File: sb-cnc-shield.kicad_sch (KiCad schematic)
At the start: 62 parts, among them P1 XMOT, P2 YMOT, P3 ZMOT, P4 AMOT, P5 UART, P6 I2C, P7 ES_SETUP, P8 12V-36V, SW1 RESET, U1 ARDUINO_UNO_SHIELD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

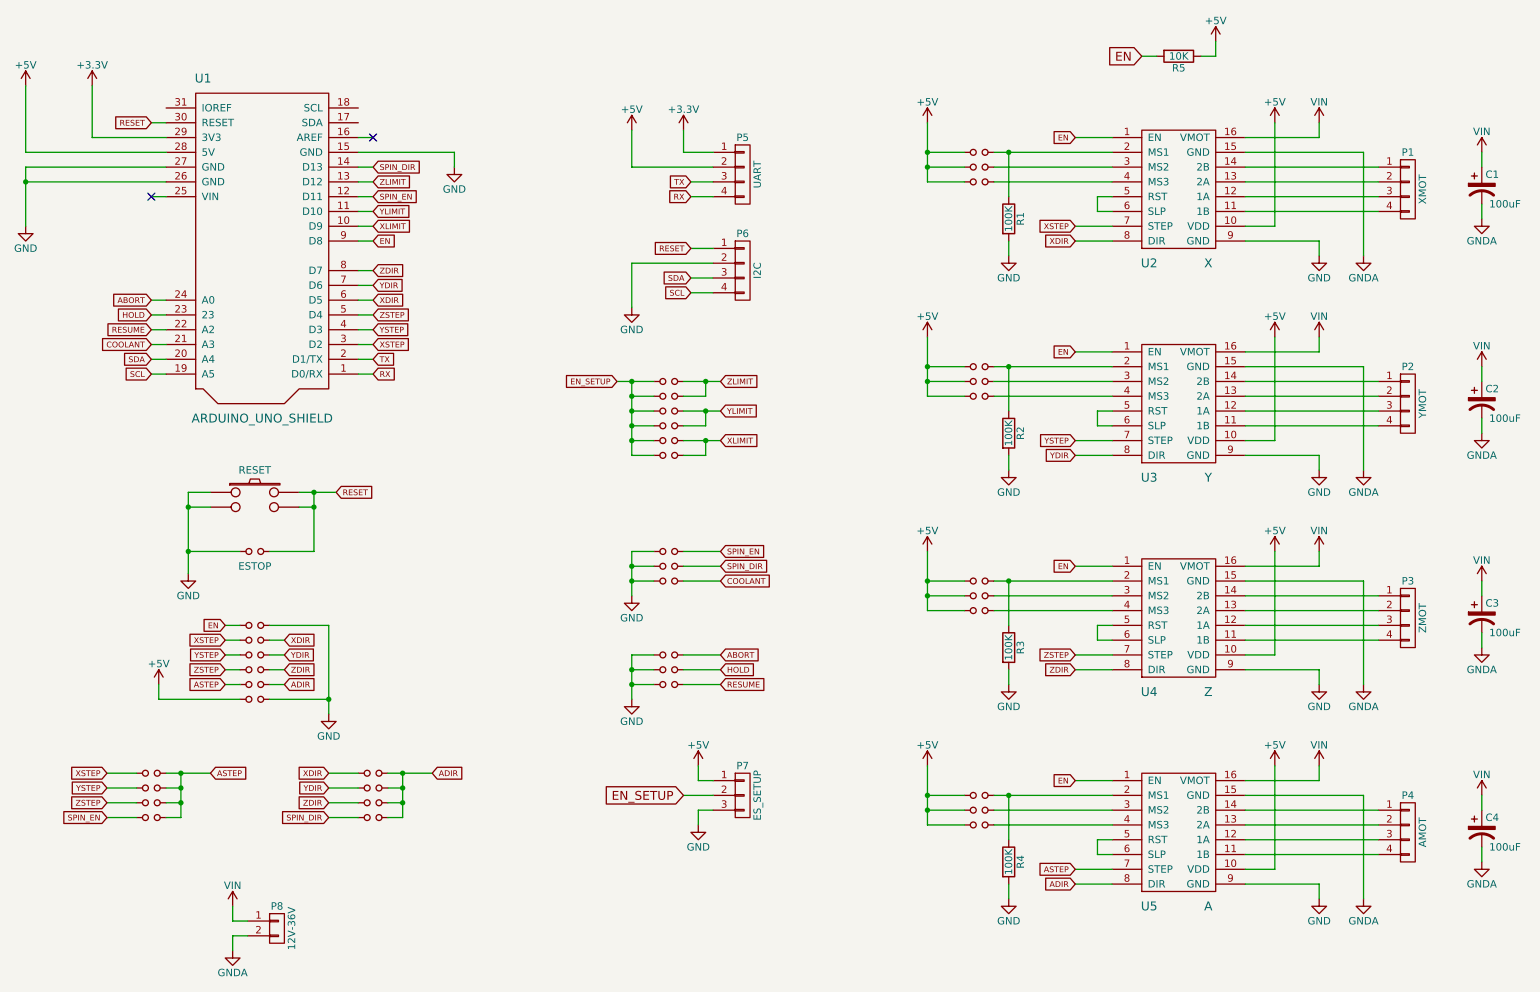
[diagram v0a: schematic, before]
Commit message: add missing prints to shield footprint
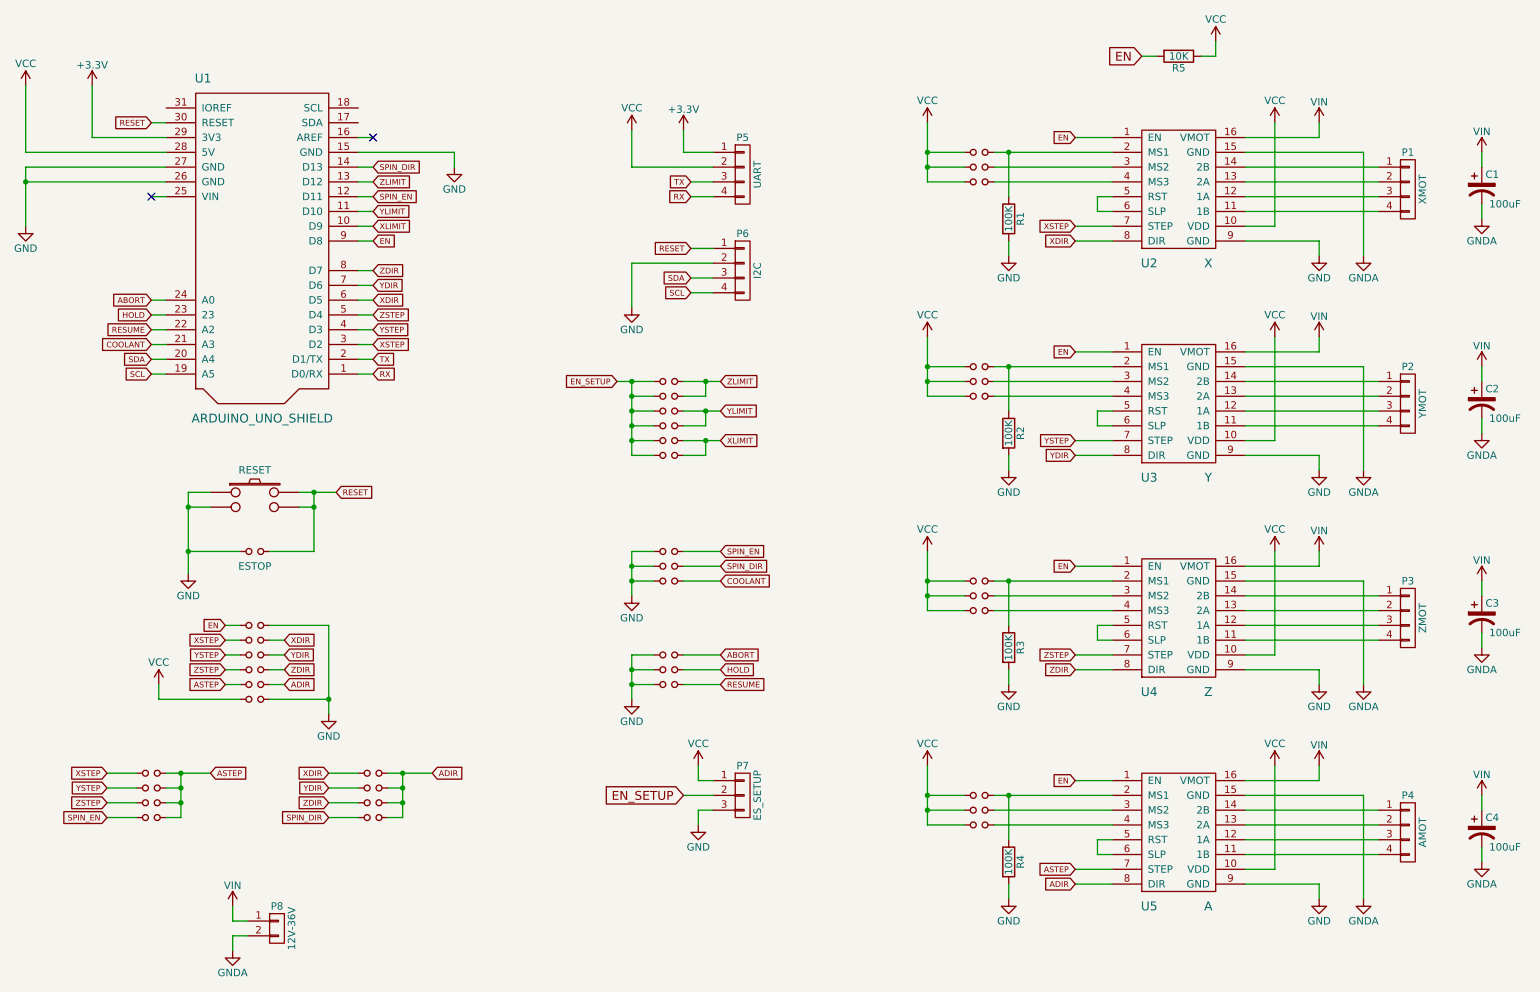
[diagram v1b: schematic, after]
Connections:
- net +5V renamed VCC

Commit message: actually properly update shield footprint
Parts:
- JP19: value SpinEn -> SEn
- JP20: value SpinDir -> SDir
- JP21: value CoolEn -> Cool
- U1: footprint footprints:ARDUINO_SHIELD -> sb-cnc-shield:ARDUINO_SHIELD
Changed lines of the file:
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@@
       (effects (font (size 1.524 1.524)))
     )
-    (property "Footprint" "footprints:ARDUINO_SHIELD" (id 2) (at 66.04 24.13 0)
+    (property "Footprint" "sb-cnc-shield:ARDUINO_SHIELD" (id 2) (at 66.04 24.13 0)
       (effects (font (size 1.524 1.524)) hide)
     )
@@
   (symbol (lib_id "power:VCC") (at 240.03 38.1 0) (unit 1)
     (in_bom yes) (on_board yes)
-    (property "Reference" "#PWR?" (id 0) (at 240.03 41.91 0)
+    (property "Reference" "#PWR0103" (id 0) (at 240.03 41.91 0)
       (effects (font (size 1.27 1.27)) hide)
     )
@@
   (symbol (lib_id "power:VCC") (at 180.34 38.1 0) (unit 1)
     (in_bom yes) (on_board yes)
-    (property "Reference" "#PWR?" (id 0) (at 180.34 41.91 0)
+    (property "Reference" "#PWR0101" (id 0) (at 180.34 41.91 0)
       (effects (font (size 1.27 1.27)) hide)
     )
@@
   (symbol (lib_id "power:VCC") (at 240.03 74.93 0) (unit 1)
     (in_bom yes) (on_board yes)
-    (property "Reference" "#PWR?" (id 0) (at 240.03 78.74 0)
+    (property "Reference" "#PWR0105" (id 0) (at 240.03 78.74 0)
       (effects (font (size 1.27 1.27)) hide)
     )
@@
   (symbol (lib_id "power:VCC") (at 180.34 74.93 0) (unit 1)
     (in_bom yes) (on_board yes)
-    (property "Reference" "#PWR?" (id 0) (at 180.34 78.74 0)
+    (property "Reference" "#PWR0102" (id 0) (at 180.34 78.74 0)
       (effects (font (size 1.27 1.27)) hide)
     )
@@
   (symbol (lib_id "power:VCC") (at 240.03 111.76 0) (unit 1)
     (in_bom yes) (on_board yes)
-    (property "Reference" "#PWR?" (id 0) (at 240.03 115.57 0)
+    (property "Reference" "#PWR0110" (id 0) (at 240.03 115.57 0)
       (effects (font (size 1.27 1.27)) hide)
     )
@@
   (symbol (lib_id "power:VCC") (at 180.34 111.76 0) (unit 1)
     (in_bom yes) (on_board yes)
-    (property "Reference" "#PWR?" (id 0) (at 180.34 115.57 0)
+    (property "Reference" "#PWR0112" (id 0) (at 180.34 115.57 0)
       (effects (font (size 1.27 1.27)) hide)
     )
@@
   (symbol (lib_id "power:VCC") (at 180.34 148.59 0) (unit 1)
     (in_bom yes) (on_board yes)
-    (property "Reference" "#PWR?" (id 0) (at 180.34 152.4 0)
+    (property "Reference" "#PWR0111" (id 0) (at 180.34 152.4 0)
       (effects (font (size 1.27 1.27)) hide)
     )
@@
   (symbol (lib_id "power:VCC") (at 240.03 148.59 0) (unit 1)
     (in_bom yes) (on_board yes)
-    (property "Reference" "#PWR?" (id 0) (at 240.03 152.4 0)
+    (property "Reference" "#PWR0113" (id 0) (at 240.03 152.4 0)
       (effects (font (size 1.27 1.27)) hide)
     )
@@
   (symbol (lib_id "power:VCC") (at 129.54 39.37 0) (unit 1)
     (in_bom yes) (on_board yes)
-    (property "Reference" "#PWR?" (id 0) (at 129.54 43.18 0)
+    (property "Reference" "#PWR0109" (id 0) (at 129.54 43.18 0)
       (effects (font (size 1.27 1.27)) hide)
     )
@@
       (effects (font (size 1.27 1.27)) hide)
     )
-    (property "Value" "SpinEn" (id 1) (at 136.144 113.284 0)
+    (property "Value" "SEn" (id 1) (at 136.144 113.284 0)
       (effects (font (size 1.27 1.27)) hide)
     )
@@
       (effects (font (size 1.27 1.27)) hide)
     )
-    (property "Value" "SpinDir" (id 1) (at 136.144 115.824 0)
+    (property "Value" "SDir" (id 1) (at 136.144 115.824 0)
       (effects (font (size 1.27 1.27)) hide)
     )
@@
       (effects (font (size 1.27 1.27)) hide)
     )
-    (property "Value" "CoolEn" (id 1) (at 136.144 118.364 0)
+    (property "Value" "Cool" (id 1) (at 136.144 118.364 0)
       (effects (font (size 1.27 1.27)) hide)
     )
@@
   (symbol (lib_id "power:VCC") (at 25.4 31.75 0) (unit 1)
     (in_bom yes) (on_board yes)
-    (property "Reference" "#PWR?" (id 0) (at 25.4 35.56 0)
+    (property "Reference" "#PWR0107" (id 0) (at 25.4 35.56 0)
       (effects (font (size 1.27 1.27)) hide)
     )
@@
   (symbol (lib_id "power:VCC") (at 48.26 134.62 0) (unit 1)
     (in_bom yes) (on_board yes)
-    (property "Reference" "#PWR?" (id 0) (at 48.26 138.43 0)
+    (property "Reference" "#PWR0108" (id 0) (at 48.26 138.43 0)
       (effects (font (size 1.27 1.27)) hide)
     )
@@
   (symbol (lib_id "power:VCC") (at 229.87 24.13 0) (unit 1)
     (in_bom yes) (on_board yes)
-    (property "Reference" "#PWR?" (id 0) (at 229.87 27.94 0)
+    (property "Reference" "#PWR0104" (id 0) (at 229.87 27.94 0)
       (effects (font (size 1.27 1.27)) hide)
     )
@@
   (symbol (lib_id "power:VCC") (at 140.97 148.59 0) (unit 1)
     (in_bom yes) (on_board yes)
-    (property "Reference" "#PWR?" (id 0) (at 140.97 152.4 0)
+    (property "Reference" "#PWR0106" (id 0) (at 140.97 152.4 0)
       (effects (font (size 1.27 1.27)) hide)
     )
@@
       (reference "#PWR049") (unit 1) (value "GNDA") (footprint "")
     )
+    (path "/00000000-0000-0000-0000-0000564a36bc"
+      (reference "#PWR0101") (unit 1) (value "VCC") (footprint "")
+    )
+    (path "/00000000-0000-0000-0000-0000564a4f27"
+      (reference "#PWR0102") (unit 1) (value "VCC") (footprint "")
+    )
     (path "/00000000-0000-0000-0000-0000564a2ca9"
-      (reference "#PWR?") (unit 1) (value "VCC") (footprint "")
-    )
-    (path "/00000000-0000-0000-0000-0000564a36bc"
-      (reference "#PWR?") (unit 1) (value "VCC") (footprint "")
+      (reference "#PWR0103") (unit 1) (value "VCC") (footprint "")
+    )
+    (path "/00000000-0000-0000-0000-0000564e00c8"
+      (reference "#PWR0104") (unit 1) (value "VCC") (footprint "")
     )
     (path "/00000000-0000-0000-0000-0000564a4eff"
-      (reference "#PWR?") (unit 1) (value "VCC") (footprint "")
-    )
-    (path "/00000000-0000-0000-0000-0000564a4f27"
-      (reference "#PWR?") (unit 1) (value "VCC") (footprint "")
+      (reference "#PWR0105") (unit 1) (value "VCC") (footprint "")
+    )
+    (path "/00000000-0000-0000-0000-0000564e12c2"
+      (reference "#PWR0106") (unit 1) (value "VCC") (footprint "")
+    )
+    (path "/00000000-0000-0000-0000-0000564c7601"
+      (reference "#PWR0107") (unit 1) (value "VCC") (footprint "")
+    )
+    (path "/00000000-0000-0000-0000-0000564c8e63"
+      (reference "#PWR0108") (unit 1) (value "VCC") (footprint "")
+    )
+    (path "/00000000-0000-0000-0000-0000564bace3"
+      (reference "#PWR0109") (unit 1) (value "VCC") (footprint "")
     )
     (path "/00000000-0000-0000-0000-0000564a6eff"
-      (reference "#PWR?") (unit 1) (value "VCC") (footprint "")
+      (reference "#PWR0110") (unit 1) (value "VCC") (footprint "")
+    )
+    (path "/00000000-0000-0000-0000-0000564a6fab"
+      (reference "#PWR0111") (unit 1) (value "VCC") (footprint "")
     )
     (path "/00000000-0000-0000-0000-0000564a6f29"
-      (reference "#PWR?") (unit 1) (value "VCC") (footprint "")
-    )
-    (path "/00000000-0000-0000-0000-0000564a6fab"
-      (reference "#PWR?") (unit 1) (value "VCC") (footprint "")
+      (reference "#PWR0112") (unit 1) (value "VCC") (footprint "")
     )
     (path "/00000000-0000-0000-0000-0000564a706f"
-      (reference "#PWR?") (unit 1) (value "VCC") (footprint "")
-    )
-    (path "/00000000-0000-0000-0000-0000564bace3"
-      (reference "#PWR?") (unit 1) (value "VCC") (footprint "")
-    )
-    (path "/00000000-0000-0000-0000-0000564c7601"
-      (reference "#PWR?") (unit 1) (value "VCC") (footprint "")
-    )
-    (path "/00000000-0000-0000-0000-0000564c8e63"
-      (reference "#PWR?") (unit 1) (value "VCC") (footprint "")
-    )
-    (path "/00000000-0000-0000-0000-0000564e00c8"
-      (reference "#PWR?") (unit 1) (value "VCC") (footprint "")
-    )
-    (path "/00000000-0000-0000-0000-0000564e12c2"
-      (reference "#PWR?") (unit 1) (value "VCC") (footprint "")
+      (reference "#PWR0113") (unit 1) (value "VCC") (footprint "")
     )
     (path "/00000000-0000-0000-0000-0000564b89a6"
@@
     )
     (path "/00000000-0000-0000-0000-0000564bc8ad"
-      (reference "JP19") (unit 1) (value "SpinEn") (footprint "footprints:Pin_100mil_Header_Straight_1x02")
+      (reference "JP19") (unit 1) (value "SEn") (footprint "footprints:Pin_100mil_Header_Straight_1x02")
     )
     (path "/00000000-0000-0000-0000-0000564bc918"
-      (reference "JP20") (unit 1) (value "SpinDir") (footprint "footprints:Pin_100mil_Header_Straight_1x02")
+      (reference "JP20") (unit 1) (value "SDir") (footprint "footprints:Pin_100mil_Header_Straight_1x02")
     )
     (path "/00000000-0000-0000-0000-0000564bc98d"
-      (reference "JP21") (unit 1) (value "CoolEn") (footprint "footprints:Pin_100mil_Header_Straight_1x02")
+      (reference "JP21") (unit 1) (value "Cool") (footprint "footprints:Pin_100mil_Header_Straight_1x02")
     )
     (path "/00000000-0000-0000-0000-0000564bf2c2"
@@
     )
     (path "/00000000-0000-0000-0000-000056463a4a"
-      (reference "U1") (unit 1) (value "ARDUINO_UNO_SHIELD") (footprint "footprints:ARDUINO_SHIELD")
+      (reference "U1") (unit 1) (value "ARDUINO_UNO_SHIELD") (footprint "sb-cnc-shield:ARDUINO_SHIELD")
     )
     (path "/00000000-0000-0000-0000-0000564a0bda"

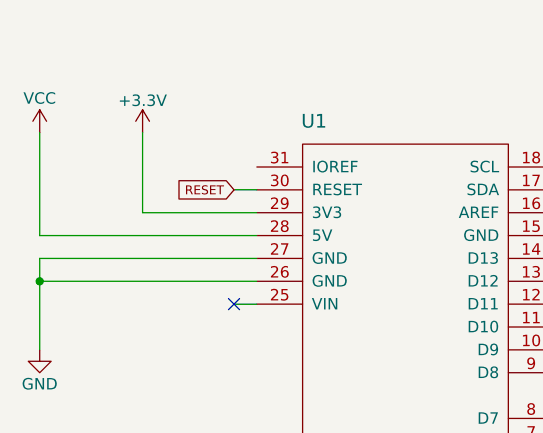
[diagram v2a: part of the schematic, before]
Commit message: reroute correctly to VCC
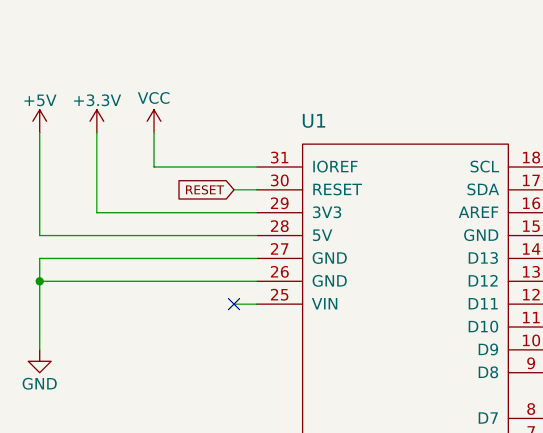
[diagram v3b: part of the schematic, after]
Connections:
- net VCC: now also U1.31 (IOREF); no longer U1.28 (5V)
- new net +5V: U1.28 (5V)
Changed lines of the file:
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@@
     (stroke (width 0) (type default) (color 0 0 0 0))
   )
-  (wire (pts (xy 36.83 40.64) (xy 49.53 40.64))
-    (stroke (width 0) (type default) (color 0 0 0 0))
-  )
   (wire (pts (xy 275.59 91.44) (xy 275.59 88.9))
     (stroke (width 0) (type default) (color 0 0 0 0))
@@
     (stroke (width 0) (type default) (color 0 0 0 0))
   )
+  (wire (pts (xy 31.75 40.64) (xy 49.53 40.64))
+    (stroke (width 0) (type default) (color 0 0 0 0))
+  )
   (wire (pts (xy 74.93 104.14) (xy 74.93 111.76))
     (stroke (width 0) (type default) (color 0 0 0 0))
@@
     (stroke (width 0) (type default) (color 0 0 0 0))
   )
+  (wire (pts (xy 25.4 31.75) (xy 25.4 43.18))
+    (stroke (width 0) (type default) (color 0 0 0 0))
+  )
   (wire (pts (xy 234.95 168.91) (xy 247.65 168.91))
     (stroke (width 0) (type default) (color 0 0 0 0))
@@
     (stroke (width 0) (type default) (color 0 0 0 0))
   )
+  (wire (pts (xy 38.1 35.56) (xy 49.53 35.56))
+    (stroke (width 0) (type default) (color 0 0 0 0))
+  )
   (wire (pts (xy 138.43 95.25) (xy 142.24 95.25))
     (stroke (width 0) (type default) (color 0 0 0 0))
@@
     (stroke (width 0) (type default) (color 0 0 0 0))
   )
-  (wire (pts (xy 36.83 31.75) (xy 36.83 40.64))
-    (stroke (width 0) (type default) (color 0 0 0 0))
-  )
   (wire (pts (xy 82.55 50.8) (xy 85.09 50.8))
     (stroke (width 0) (type default) (color 0 0 0 0))
@@
     (stroke (width 0) (type default) (color 0 0 0 0))
   )
+  (wire (pts (xy 25.4 43.18) (xy 49.53 43.18))
+    (stroke (width 0) (type default) (color 0 0 0 0))
+  )
   (wire (pts (xy 234.95 121.92) (xy 257.81 121.92))
     (stroke (width 0) (type default) (color 0 0 0 0))
@@
     (stroke (width 0) (type default) (color 0 0 0 0))
   )
-  (wire (pts (xy 25.4 31.75) (xy 25.4 43.18))
-    (stroke (width 0) (type default) (color 0 0 0 0))
-  )
   (wire (pts (xy 129.54 134.62) (xy 129.54 137.16))
     (stroke (width 0) (type default) (color 0 0 0 0))
@@
     (stroke (width 0) (type default) (color 0 0 0 0))
   )
+  (wire (pts (xy 31.75 31.75) (xy 31.75 40.64))
+    (stroke (width 0) (type default) (color 0 0 0 0))
+  )
   (wire (pts (xy 275.59 45.72) (xy 275.59 43.18))
     (stroke (width 0) (type default) (color 0 0 0 0))
@@
     (stroke (width 0) (type default) (color 0 0 0 0))
   )
-  (wire (pts (xy 25.4 43.18) (xy 49.53 43.18))
-    (stroke (width 0) (type default) (color 0 0 0 0))
-  )
   (wire (pts (xy 257.81 45.72) (xy 234.95 45.72))
     (stroke (width 0) (type default) (color 0 0 0 0))
@@
     (stroke (width 0) (type default) (color 0 0 0 0))
   )
+  (wire (pts (xy 38.1 31.75) (xy 38.1 35.56))
+    (stroke (width 0) (type default) (color 0 0 0 0))
+  )
   (wire (pts (xy 53.34 101.6) (xy 53.34 104.14))
     (stroke (width 0) (type default) (color 0 0 0 0))
@@
     (pin "1")
   )
-  (symbol (lib_id "power:+3.3V") (at 36.83 31.75 0) (unit 1)
+  (symbol (lib_id "power:+3.3V") (at 31.75 31.75 0) (unit 1)
     (in_bom yes) (on_board yes)
-    (property "Reference" "#PWR032" (id 0) (at 36.83 35.56 0)
+    (property "Reference" "#PWR032" (id 0) (at 31.75 35.56 0)
       (effects (font (size 1.27 1.27)) hide)
     )
-    (property "Value" "+3.3V" (id 1) (at 36.83 28.194 0))
-    (property "Footprint" "" (id 2) (at 36.83 31.75 0)
+    (property "Value" "+3.3V" (id 1) (at 31.75 28.194 0))
+    (property "Footprint" "" (id 2) (at 31.75 31.75 0)
       (effects (font (size 1.524 1.524)))
     )
-    (property "Datasheet" "" (id 3) (at 36.83 31.75 0)
+    (property "Datasheet" "" (id 3) (at 31.75 31.75 0)
       (effects (font (size 1.524 1.524)))
     )
     (pin "1")
   )
-  (symbol (lib_id "power:VCC") (at 25.4 31.75 0) (unit 1)
+  (symbol (lib_id "power:VCC") (at 38.1 31.75 0) (unit 1)
     (in_bom yes) (on_board yes)
-    (property "Reference" "#PWR0107" (id 0) (at 25.4 35.56 0)
+    (property "Reference" "#PWR0107" (id 0) (at 38.1 35.56 0)
       (effects (font (size 1.27 1.27)) hide)
     )
-    (property "Value" "VCC" (id 1) (at 25.4 27.94 0))
-    (property "Footprint" "" (id 2) (at 25.4 31.75 0)
+    (property "Value" "VCC" (id 1) (at 38.1 27.94 0))
+    (property "Footprint" "" (id 2) (at 38.1 31.75 0)
       (effects (font (size 1.27 1.27)) hide)
     )
-    (property "Datasheet" "" (id 3) (at 25.4 31.75 0)
+    (property "Datasheet" "" (id 3) (at 38.1 31.75 0)
       (effects (font (size 1.27 1.27)) hide)
     )
@@
     (pin "1")
   )
+  (symbol (lib_id "power:+5V") (at 25.4 31.75 0) (unit 1)
+    (in_bom yes) (on_board yes)
+    (property "Reference" "#PWR?" (id 0) (at 25.4 35.56 0)
+      (effects (font (size 1.27 1.27)) hide)
+    )
+    (property "Value" "+5V" (id 1) (at 25.4 28.194 0))
+    (property "Footprint" "" (id 2) (at 25.4 31.75 0)
+      (effects (font (size 1.27 1.27)) hide)
+    )
+    (property "Datasheet" "" (id 3) (at 25.4 31.75 0)
+      (effects (font (size 1.27 1.27)) hide)
+    )
+    (pin "1")
+  )
   (sheet_instances
     (path "/" (page "1"))
@@
       (reference "#PWR0113") (unit 1) (value "VCC") (footprint "")
     )
+    (path "/162c9947-354e-42e4-8cf3-b34290a8f293"
+      (reference "#PWR?") (unit 1) (value "+5V") (footprint "")
+    )
     (path "/00000000-0000-0000-0000-0000564b89a6"
